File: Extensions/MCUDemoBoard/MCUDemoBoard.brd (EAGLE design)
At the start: 117.6 x 67 mm, 23 parts, among them J1 CONN_20X2NOSILK, SW1 SPST_TACT-KMR2, U1 ATSAMD21J18A-AUT, U6 MAX3232, X4 NX3215SA-32.768K-STD-MUA-8

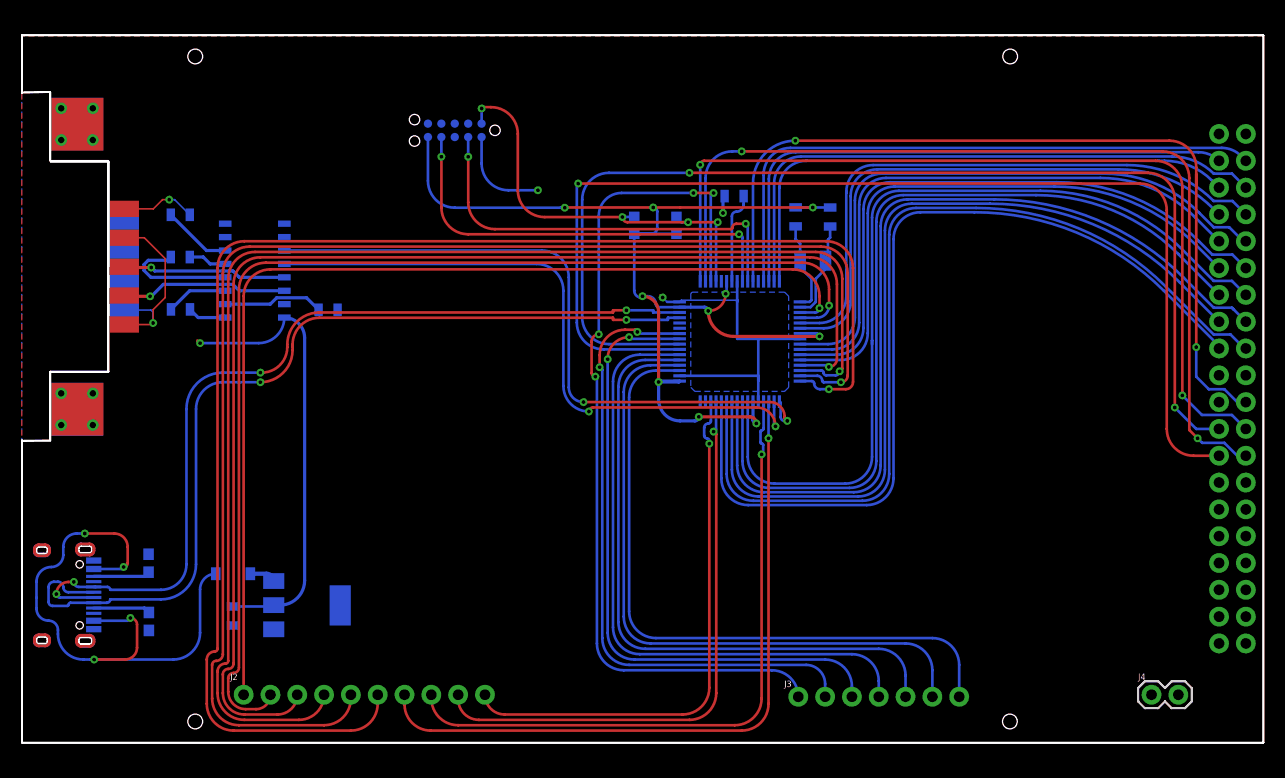
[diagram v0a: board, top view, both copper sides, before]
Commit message: changed MCU test board for FPC cable, other mods, moved test keyboard
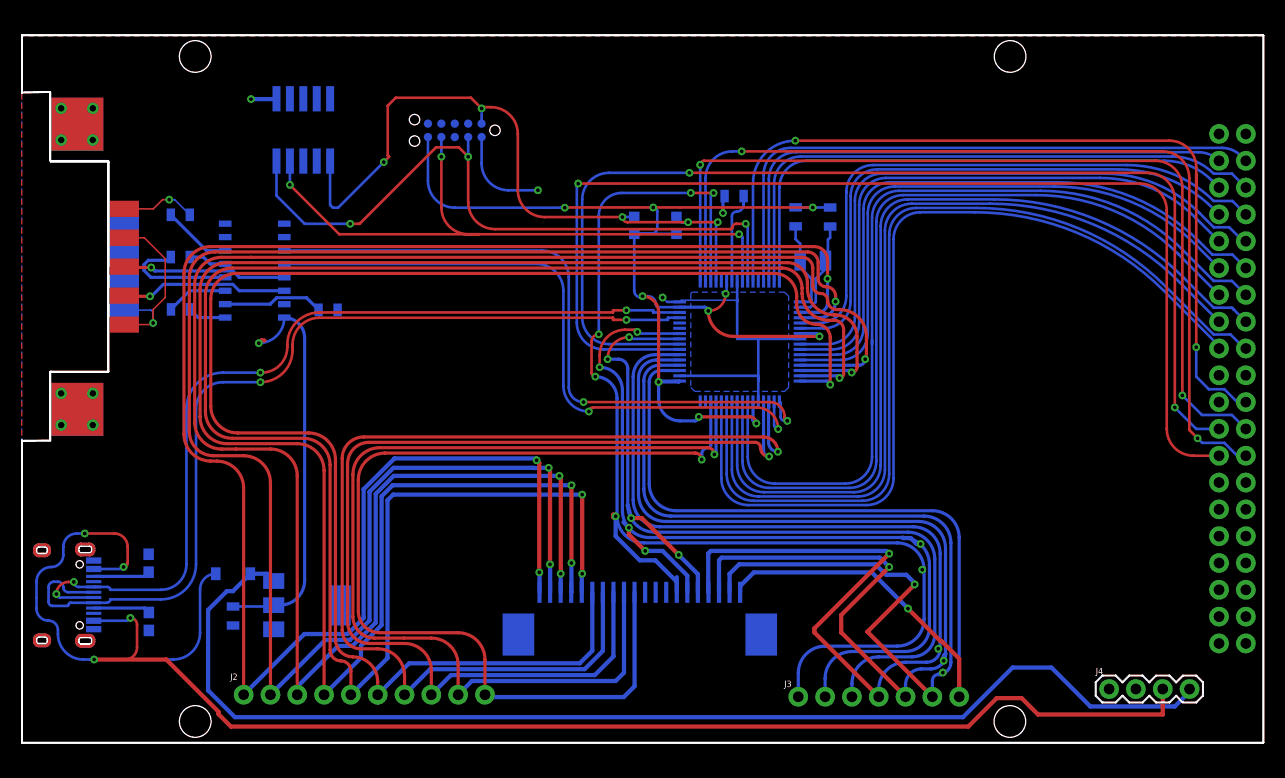
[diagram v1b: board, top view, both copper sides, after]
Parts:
- added U$1: FC1-20-L2-T-WT20PIN, FPC:FC1-20-L2-T-WT
- added X1: 1365-10, con-leotronics:1365-10
- J4: device SparkFun-Connectors:1X02 -> SparkFun-Connectors:1X04
- moved J4 4.06 mm to (102.9, 5.08)
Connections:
- net 3V3: now also X1.1
- net GND: now also X1.3, X1.5, X1.9
- net KEYCOLUM0: now also U$1.20
- net KEYCOLUM1: now also U$1.19
- net KEYCOLUM2: now also U$1.18
- net KEYCOLUM3: now also U$1.17
- net KEYCOLUM4: now also U$1.16
- net KEYCOLUM5: now also U$1.15
- net KEYCOLUM6: now also U$1.14
- net KEYROW0: now also U$1.1
- net KEYROW1: now also U$1.2
- net KEYROW2: now also U$1.3
- net KEYROW3: now also U$1.4
- net KEYROW4: now also U$1.5
- net KEYROW5: now also U$1.6
- net KEYROW6: now also U$1.7
- net KEYROW7: now also U$1.8
- net KEYROW8: now also U$1.9
- net KEYROW9: now also U$1.10
- net N$2: now also J4.4
- net RESET: now also X1.10
- net SWCLK: now also X1.4
- net SWDIO: now also X1.2
- net VUSB: now also J4.3
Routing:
- net N$2: track 2.50 -> 113.9 mm
- net VUSB: track 55.5 -> 163.7 mm
- net KEYROW0: track 97.6 -> 169.1 mm, vias 1 -> 3
- net KEYROW1: track 106.5 -> 168.0 mm, vias 1 -> 3
- net KEYROW2: track 118.0 -> 175.4 mm, vias 1 -> 3
- net KEYROW3: track 125.0 -> 171.8 mm, vias 1 -> 3
- net KEYCOLUM3: track 59.4 -> 105.5 mm, vias 0 -> 2
- net KEYROW9: track 50.6 -> 92.9 mm
- net KEYCOLUM2: track 60.4 -> 100.0 mm, vias 0 -> 2
- net KEYROW8: track 54.5 -> 93.0 mm
- net KEYROW7: track 62.1 -> 98.7 mm
- net KEYROW4: track 132.3 -> 168.1 mm, vias 1 -> 3
- net KEYCOLUM1: track 61.5 -> 96.8 mm, vias 0 -> 2
- net KEYROW6: track 66.1 -> 99.6 mm
- net KEYCOLUM6: track 82.6 -> 113.9 mm, vias 4 -> 6
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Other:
- board text added: "5V In"
- board text added: "VUSB"

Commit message: Added SamD51 demo board; tried to get D51 software working
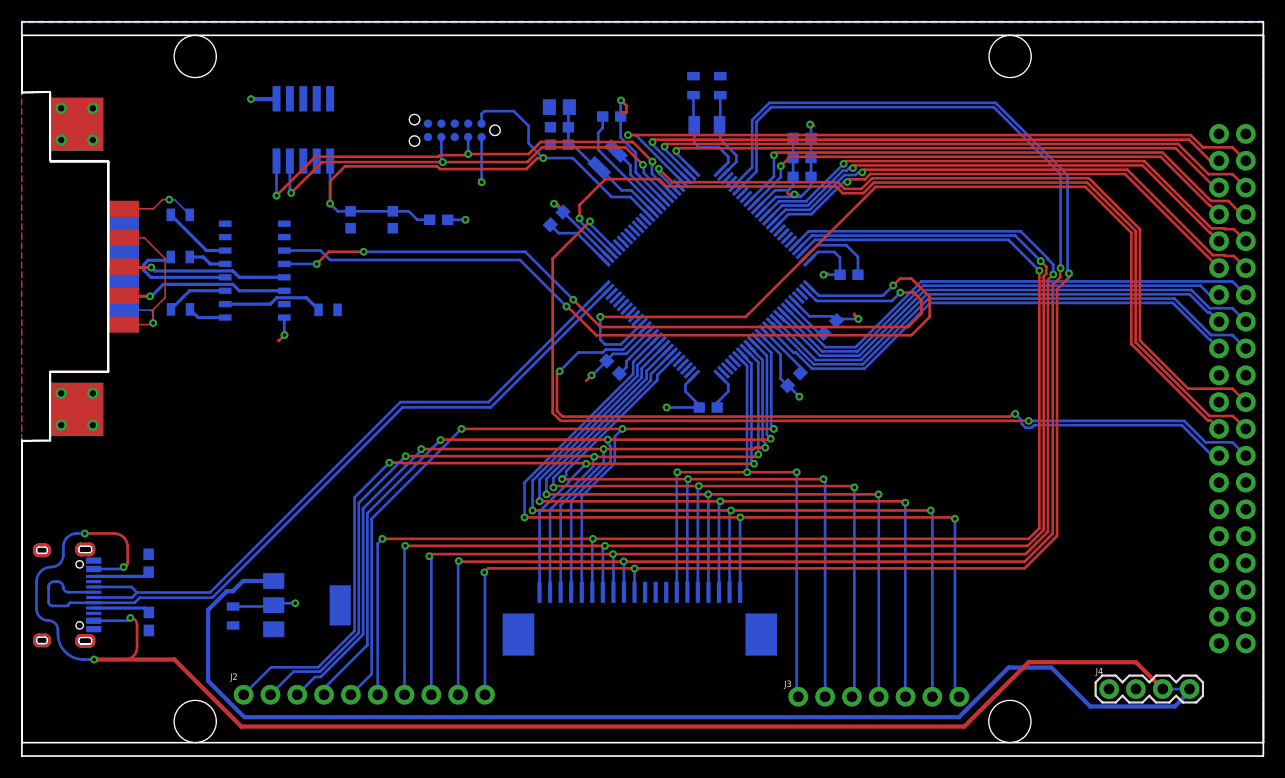
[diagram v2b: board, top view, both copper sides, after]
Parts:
- removed C12: 1.0uF, SparkFun-Capacitors:0805
- removed C26, C27: 22pF, SparkFun-Capacitors:0805
- removed D1: MBR120, adafruit:SOD-123FL
- removed SW1: SPST_TACT-KMR2, adafruit:KMR2
- removed U1: ATSAMD21J18A-AUT, ATSam21:TQFP64-10X10
- removed X4: NX3215SA-32.768K-STD-MUA-8, adafruit2:XTAL3215
- added C1, C2: 22pF, SparkFun-Capacitors:0805
- added C14: 10uF, microbuilder:0805-NO
- added C15: 1uF, microbuilder:0603-NO
- added C16, C17, C18, C19, C20, C21, C25, C28, C29, C30, C31: .1u, microbuilder:0603-NO
- added IC1: ATSAMD51N19A-AU, SamacSys_Parts:QFP50P1600X1600X120-100N
- added L3: 10uH, microbuilder:INDUCTOR_1007
- added R15: 10K, microbuilder:0603-NO
- added SW2: SPST_TACT-KMR2, adafruit:KMR2
- added X2: NX3215SA-32.768K-STD-MUA-8, adafruit2:XTAL3215
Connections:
- removed net N$2: D1.C, J4.4, VREG.3
- removed net N$3: C12.1, U1.55
- removed net N$54: C26.1, U1.1, X4.P$1
- removed net N$55: C27.1, U1.2, X4.P$2
- removed net PB31: U1.60
- removed net SERCOM3_PAD0: U1.43
- removed net SERCOM3_PAD1: U1.44
- new net N$26: C14.1, C15.1, C16.2, IC1.89, L3.P$1
- new net N$27: IC1.91, L3.P$2
- new net N$4: C2.2, IC1.1, X2.P$1
- new net N$5: C1.2, IC1.2, X2.P$2
- net 3V3: now also C17.2, C18.2, C19.2, C20.2, C21.2, C25.2, C28.2, C29.2, C30.2, C31.2, IC1.12, IC1.25, IC1.30, IC1.39, IC1.51, IC1.63, IC1.77, IC1.92, R15.1; no longer U1.21, U1.34, U1.48, U1.56, U1.8
- net GND: now also C1.1, C14.2, C15.2, C16.1, C17.1, C18.1, C19.1, C2.1, C20.1, C21.1, C25.1, C28.1, C29.1, C30.1, C31.1, IC1.11, IC1.24, IC1.31, IC1.38, IC1.50, IC1.62, IC1.76, IC1.90, SW2.2, SW2.4; no longer C12.2, C26.2, C27.2, SW1.2, SW1.4, U1.22, U1.33, U1.47, U1.54, U1.7
- net KEYCOLUM0: now also IC1.61; no longer U1.35
- net KEYCOLUM1: now also IC1.60; no longer U1.36
- net KEYCOLUM2: now also IC1.59; no longer U1.37
- net KEYCOLUM3: now also IC1.58; no longer U1.38
- net KEYCOLUM4: now also IC1.57; no longer U1.41
- net KEYCOLUM5: now also IC1.56; no longer U1.42
- net KEYCOLUM6: now also IC1.45; no longer U1.51
- net KEYROW0: now also IC1.44; no longer U1.3
- net KEYROW1: now also IC1.43; no longer U1.4
- net KEYROW2: now also IC1.42; no longer U1.13
- net KEYROW3: now also IC1.41; no longer U1.14
- net KEYROW4: now also IC1.40; no longer U1.15
- net KEYROW5: now also IC1.23; no longer U1.16
- net KEYROW6: now also IC1.22; no longer U1.19
- net KEYROW7: now also IC1.21; no longer U1.20
- net KEYROW8: now also IC1.6; no longer U1.29
- net KEYROW9: now also IC1.5; no longer U1.30
- net LCD0: now also IC1.97; no longer U1.61
- net LCD1: now also IC1.98; no longer U1.62
- net LCD10: now also IC1.32; no longer U1.23
- net LCD11: now also IC1.33; no longer U1.24
- net LCD12: now also IC1.34; no longer U1.25
- net LCD13: now also IC1.35; no longer U1.26
- net LCD14: now also IC1.36; no longer U1.27
- net LCD15: now also IC1.37; no longer U1.28
- net LCD2: now also IC1.99; no longer U1.63
- net LCD3: now also IC1.100; no longer U1.64
- net LCD4: now also IC1.9; no longer U1.5
- net LCD5: now also IC1.10; no longer U1.6
- net LCD6: now also IC1.13; no longer U1.9
- net LCD7: now also IC1.14; no longer U1.10
- net LCD8: now also IC1.15; no longer U1.11
- net LCD9: now also IC1.16; no longer U1.12
- net LCD_CS: now also IC1.78; no longer U1.49
- net LCD_D/C: now also IC1.79; no longer U1.50
- net LCD_RD: now also IC1.64; no longer U1.39
- net LCD_RESET: now also IC1.95; no longer U1.59
- net LCD_W/R: now also IC1.65; no longer U1.40
- net RESET: now also IC1.88, R15.2, SW2.1, SW2.3; no longer SW1.1, SW1.3, U1.52
- net SWCLK: now also IC1.93; no longer U1.57
- net SWDIO: now also IC1.94; no longer U1.58
- net UART_RX: now also IC1.27; no longer U1.18
- net UART_TX: now also IC1.26; no longer U1.17
- net USB_N: now also IC1.74; no longer U1.45
- net USB_P: now also IC1.75; no longer U1.46
- net VUSB: now also J4.4, VREG.3; no longer D1.A
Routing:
- net N$2: track 113.9 -> 0.00 mm
- net VUSB: track 163.7 -> 261.0 mm
- net KEYROW2: track 175.4 -> 86.6 mm
- net KEYROW3: track 171.8 -> 86.5 mm
- net KEYROW4: track 168.1 -> 85.4 mm
- net KEYROW1: track 168.0 -> 87.9 mm
- net KEYROW0: track 169.1 -> 89.8 mm
- net GND: track 125.1 -> 59.7 mm, vias 12 -> 1
- net KEYCOLUM6: track 113.9 -> 55.3 mm, vias 6 -> 3
- net KEYROW8: track 93.0 -> 146.6 mm, vias 1 -> 3
- net KEYROW9: track 92.9 -> 145.1 mm, vias 1 -> 3
- net LCD15: track 84.1 -> 48.7 mm
- net LCD14: track 85.8 -> 51.0 mm
- net LCD13: track 81.4 -> 47.2 mm
- net LCD12: track 83.4 -> 49.5 mm
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- removed copper zone on layer 16, net 3V3
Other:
- board size 117.6 x 67 mm -> 117.6 x 69.5 mm
